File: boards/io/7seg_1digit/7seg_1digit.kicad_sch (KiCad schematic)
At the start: 12 parts, among them J1 Conn_01x06, J2 ~{MCLR}, U1 PIC16F1503-ISL, U2 OSL10561-LRA

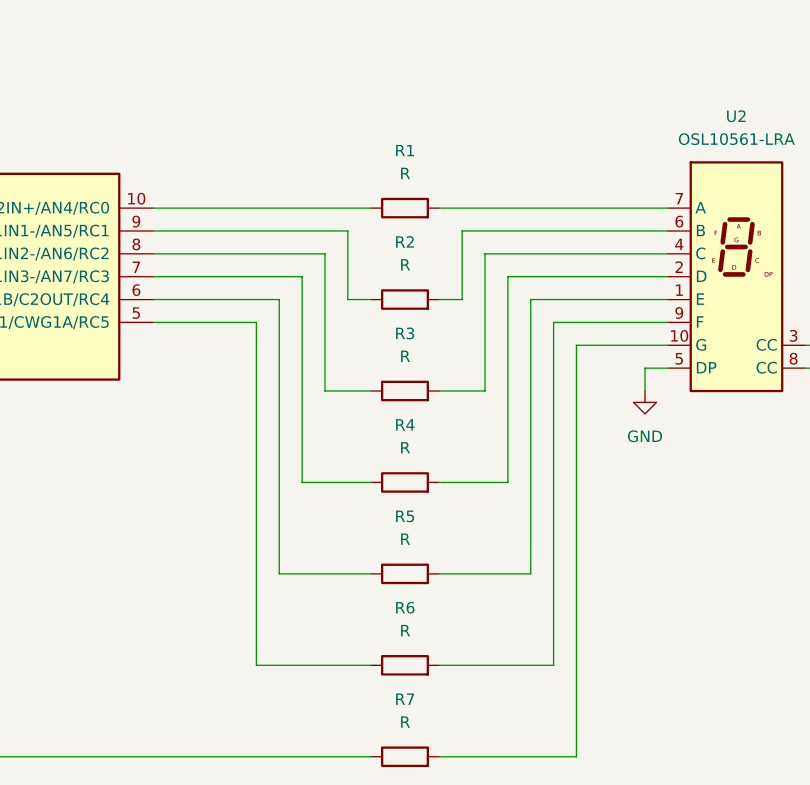
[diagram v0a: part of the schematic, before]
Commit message: set resistor values
* 7seg_1digit
* 7seg_3digits
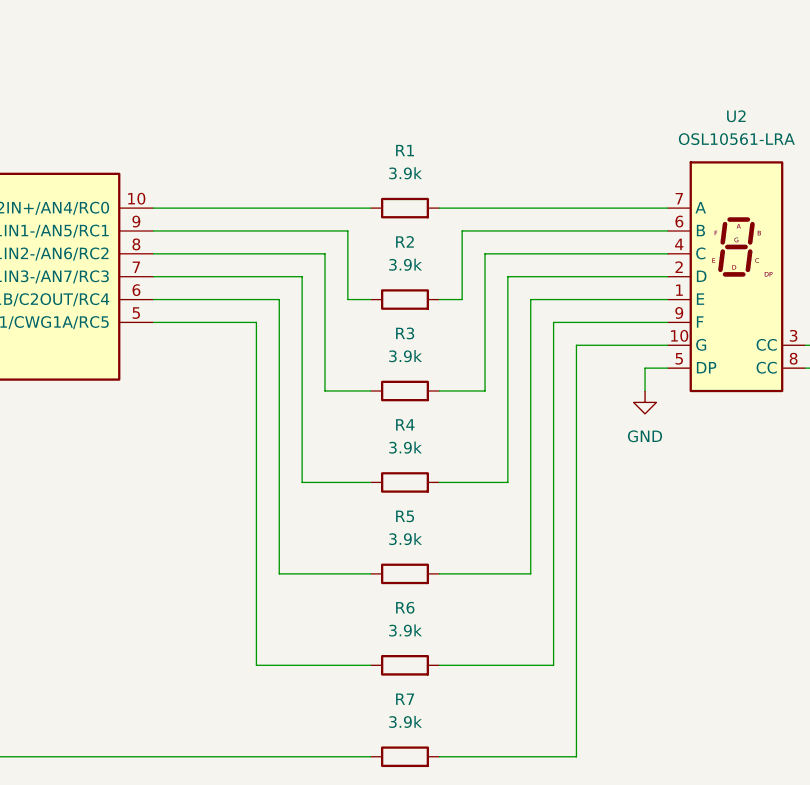
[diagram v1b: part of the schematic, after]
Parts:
- R1, R2, R3, R4, R5, R6, R7: value R -> 3.9k
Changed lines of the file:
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@@
     (in_bom yes) (on_board yes) (fields_autoplaced)
     (property "Reference" "R2" (id 0) (at 223.52 78.74 90))
-    (property "Value" "R" (id 1) (at 223.52 81.28 90))
+    (property "Value" "3.9k" (id 1) (at 223.52 81.28 90))
     (property "Footprint" "Resistor_SMD:R_0805_2012Metric_Pad1.20x1.40mm_HandSolder" (id 2) (at 223.52 86.868 90)
       (effects (font (size 1.27 1.27)) hide)
@@
     (in_bom yes) (on_board yes) (fields_autoplaced)
     (property "Reference" "R3" (id 0) (at 223.52 88.9 90))
-    (property "Value" "R" (id 1) (at 223.52 91.44 90))
+    (property "Value" "3.9k" (id 1) (at 223.52 91.44 90))
     (property "Footprint" "Resistor_SMD:R_0805_2012Metric_Pad1.20x1.40mm_HandSolder" (id 2) (at 223.52 97.028 90)
       (effects (font (size 1.27 1.27)) hide)
@@
     (in_bom yes) (on_board yes) (fields_autoplaced)
     (property "Reference" "R6" (id 0) (at 223.52 119.38 90))
-    (property "Value" "R" (id 1) (at 223.52 121.92 90))
+    (property "Value" "3.9k" (id 1) (at 223.52 121.92 90))
     (property "Footprint" "Resistor_SMD:R_0805_2012Metric_Pad1.20x1.40mm_HandSolder" (id 2) (at 223.52 127.508 90)
       (effects (font (size 1.27 1.27)) hide)
@@
     (in_bom yes) (on_board yes) (fields_autoplaced)
     (property "Reference" "R7" (id 0) (at 223.52 129.54 90))
-    (property "Value" "R" (id 1) (at 223.52 132.08 90))
+    (property "Value" "3.9k" (id 1) (at 223.52 132.08 90))
     (property "Footprint" "Resistor_SMD:R_0805_2012Metric_Pad1.20x1.40mm_HandSolder" (id 2) (at 223.52 137.668 90)
       (effects (font (size 1.27 1.27)) hide)
@@
     (in_bom yes) (on_board yes) (fields_autoplaced)
     (property "Reference" "R1" (id 0) (at 223.52 68.58 90))
-    (property "Value" "R" (id 1) (at 223.52 71.12 90))
+    (property "Value" "3.9k" (id 1) (at 223.52 71.12 90))
     (property "Footprint" "Resistor_SMD:R_0805_2012Metric_Pad1.20x1.40mm_HandSolder" (id 2) (at 223.52 76.708 90)
       (effects (font (size 1.27 1.27)) hide)
@@
     (in_bom yes) (on_board yes) (fields_autoplaced)
     (property "Reference" "R5" (id 0) (at 223.52 109.22 90))
-    (property "Value" "R" (id 1) (at 223.52 111.76 90))
+    (property "Value" "3.9k" (id 1) (at 223.52 111.76 90))
     (property "Footprint" "Resistor_SMD:R_0805_2012Metric_Pad1.20x1.40mm_HandSolder" (id 2) (at 223.52 117.348 90)
       (effects (font (size 1.27 1.27)) hide)
@@
     (in_bom yes) (on_board yes) (fields_autoplaced)
     (property "Reference" "R4" (id 0) (at 223.52 99.06 90))
-    (property "Value" "R" (id 1) (at 223.52 101.6 90))
+    (property "Value" "3.9k" (id 1) (at 223.52 101.6 90))
     (property "Footprint" "Resistor_SMD:R_0805_2012Metric_Pad1.20x1.40mm_HandSolder" (id 2) (at 223.52 107.188 90)
       (effects (font (size 1.27 1.27)) hide)
@@
     )
     (path "/8d1e9f7e-d56d-499a-b443-f648043686a9"
-      (reference "R1") (unit 1) (value "R") (footprint "Resistor_SMD:R_0805_2012Metric_Pad1.20x1.40mm_HandSolder")
+      (reference "R1") (unit 1) (value "3.9k") (footprint "Resistor_SMD:R_0805_2012Metric_Pad1.20x1.40mm_HandSolder")
     )
     (path "/0283b9ce-2dd6-4090-ab5e-478466ed0609"
-      (reference "R2") (unit 1) (value "R") (footprint "Resistor_SMD:R_0805_2012Metric_Pad1.20x1.40mm_HandSolder")
+      (reference "R2") (unit 1) (value "3.9k") (footprint "Resistor_SMD:R_0805_2012Metric_Pad1.20x1.40mm_HandSolder")
     )
     (path "/4a453a24-28ca-499a-b93c-998f0a8f8cbb"
-      (reference "R3") (unit 1) (value "R") (footprint "Resistor_SMD:R_0805_2012Metric_Pad1.20x1.40mm_HandSolder")
+      (reference "R3") (unit 1) (value "3.9k") (footprint "Resistor_SMD:R_0805_2012Metric_Pad1.20x1.40mm_HandSolder")
     )
     (path "/b30478a8-778e-4998-8f96-42e2a452e894"
-      (reference "R4") (unit 1) (value "R") (footprint "Resistor_SMD:R_0805_2012Metric_Pad1.20x1.40mm_HandSolder")
+      (reference "R4") (unit 1) (value "3.9k") (footprint "Resistor_SMD:R_0805_2012Metric_Pad1.20x1.40mm_HandSolder")
     )
     (path "/a767c7d1-d95b-4a49-85ba-1c89e8982f59"
-      (reference "R5") (unit 1) (value "R") (footprint "Resistor_SMD:R_0805_2012Metric_Pad1.20x1.40mm_HandSolder")
+      (reference "R5") (unit 1) (value "3.9k") (footprint "Resistor_SMD:R_0805_2012Metric_Pad1.20x1.40mm_HandSolder")
     )
     (path "/4acc2ae9-1bb4-4de4-a29f-61b58b7cd7dd"
-      (reference "R6") (unit 1) (value "R") (footprint "Resistor_SMD:R_0805_2012Metric_Pad1.20x1.40mm_HandSolder")
+      (reference "R6") (unit 1) (value "3.9k") (footprint "Resistor_SMD:R_0805_2012Metric_Pad1.20x1.40mm_HandSolder")
     )
     (path "/763b9938-f742-4868-bc2c-07e59973ae73"
-      (reference "R7") (unit 1) (value "R") (footprint "Resistor_SMD:R_0805_2012Metric_Pad1.20x1.40mm_HandSolder")
+      (reference "R7") (unit 1) (value "3.9k") (footprint "Resistor_SMD:R_0805_2012Metric_Pad1.20x1.40mm_HandSolder")
     )
     (path "/03cc8415-eebf-4a5c-ab19-44f88336b0b6"
